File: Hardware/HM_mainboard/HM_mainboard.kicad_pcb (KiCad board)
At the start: 2 copper layers, 80 x 55 mm, 58 parts, among them J1 JST PH2P ST90, J2 USB4105-GF-A, J3 Conn_01x04, J4 54-00174, J5 54-00174, J6 54-00174, J7 54-00174, Q1 PMOS AS3401, U1 MCP73831-2, U2 TC1262-33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

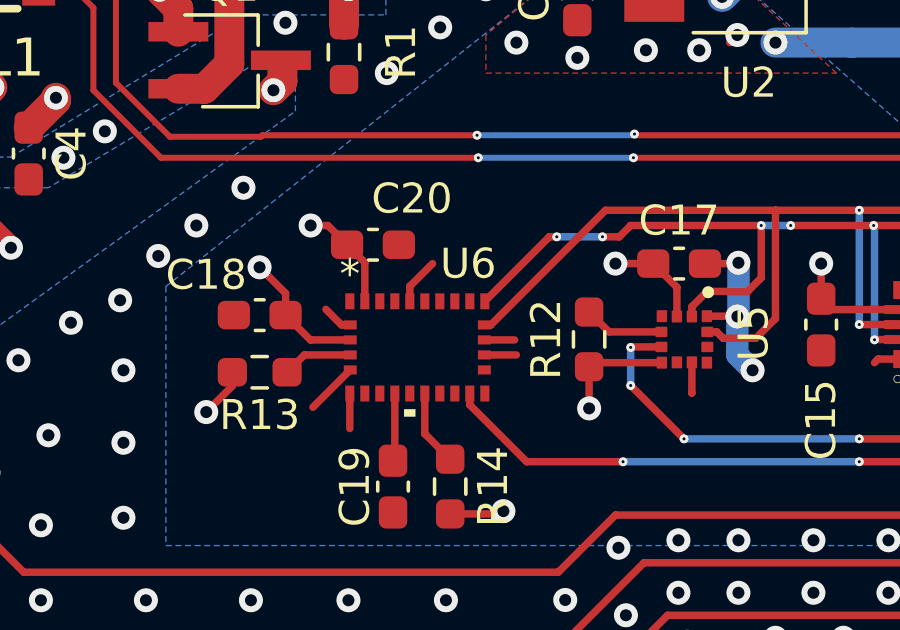
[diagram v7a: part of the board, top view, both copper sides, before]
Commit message: Fixed missing GND connections of BNO055 at Pin 15 and 16
Bugfix due to wrong pin assignments in symbol library
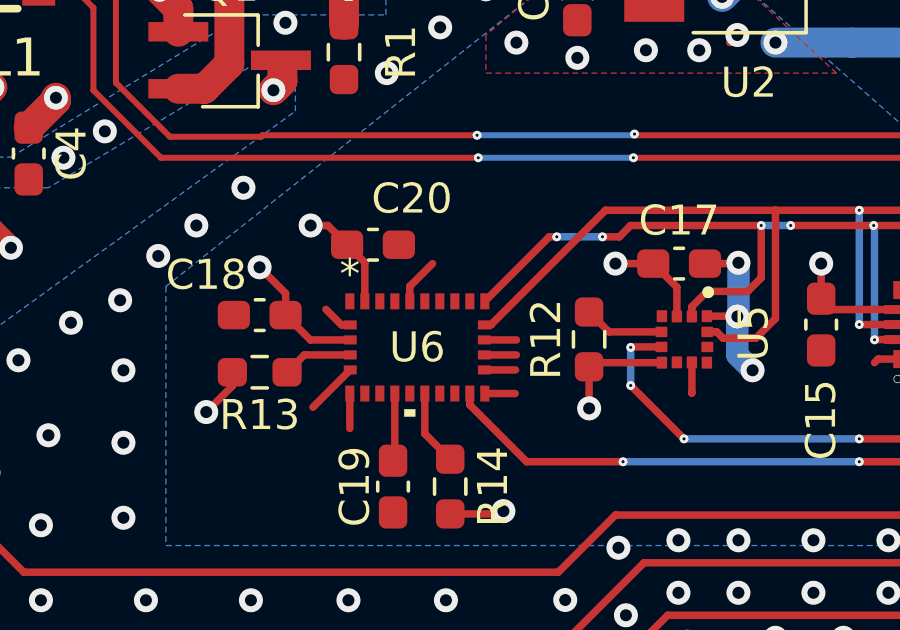
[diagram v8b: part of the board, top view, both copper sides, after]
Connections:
- U6 pad 15: unconnected-(U6-NC-Pad15) -> GND
- U6 pad 16: unconnected-(U6-NC-Pad16) -> GND
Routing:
- net GND: track 30.7 -> 32.8 mm
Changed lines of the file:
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@@
   (net 73 "unconnected-(U6-NC-Pad12)")
   (net 74 "unconnected-(U6-NC-Pad13)")
-  (net 75 "unconnected-(U6-NC-Pad15)")
-  (net 76 "unconnected-(U6-NC-Pad16)")
-  (net 77 "unconnected-(U6-NC-Pad21)")
-  (net 78 "unconnected-(U6-NC-Pad22)")
-  (net 79 "unconnected-(U6-NC-Pad23)")
-  (net 80 "unconnected-(U6-NC-Pad24)")
-  (net 81 "unconnected-(U6-XOUT32-Pad26)")
-  (net 82 "unconnected-(U6-XIN32-Pad27)")
+  (net 75 "unconnected-(U6-NC-Pad21)")
+  (net 76 "unconnected-(U6-NC-Pad22)")
+  (net 77 "unconnected-(U6-NC-Pad23)")
+  (net 78 "unconnected-(U6-NC-Pad24)")
+  (net 79 "unconnected-(U6-XOUT32-Pad26)")
+  (net 80 "unconnected-(U6-XIN32-Pad27)")
   (footprint "Capacitor_SMD:C_0603_1608Metric_Pad1.08x0.95mm_HandSolder" (layer "F.Cu")
     (at 166.116 99.06 90)
@@
     (property "ki_keywords" "BNO055")
     (attr smd)
-    (fp_text reference "U6" (at 1.697499 -2.7883 unlocked) (layer "F.SilkS")
+    (fp_text reference "U6" (at 0 0 unlocked) (layer "F.SilkS")
         (effects (font (size 1 1) (thickness 0.15)))
     )
@@
       (net 51 "/BNO55_INT") (pinfunction "INT") (pintype "output"))
     (pad "15" smd rect (at 2.249999 1.5367) (size 0.3048 0.5334) (layers "F.Cu" "F.Paste" "F.Mask")
-      (net 75 "unconnected-(U6-NC-Pad15)") (pinfunction "NC") (pintype "no_connect"))
+      (net 1 "GND") (pinfunction "Pin15") (pintype "power_out"))
     (pad "16" smd rect (at 2.2352 0.750001 90) (size 0.3048 0.4318) (layers "F.Cu" "F.Paste" "F.Mask")
-      (net 76 "unconnected-(U6-NC-Pad16)") (pinfunction "NC") (pintype "no_connect"))
+      (net 1 "GND") (pinfunction "Pin16") (pintype "power_out"))
     (pad "17" smd rect (at 2.2352 0.25 90) (size 0.3048 0.4318) (layers "F.Cu" "F.Paste" "F.Mask")
       (net 1 "GND") (pinfunction "COM3") (pintype "input"))
@@
       (net 8 "/I2C_SDA") (pinfunction "COM0") (pintype "bidirectional"))
     (pad "21" smd rect (at 1.749999 -1.5367) (size 0.3048 0.5334) (layers "F.Cu" "F.Paste" "F.Mask")
-      (net 77 "unconnected-(U6-NC-Pad21)") (pinfunction "NC") (pintype "no_connect"))
+      (net 75 "unconnected-(U6-NC-Pad21)") (pinfunction "NC") (pintype "no_connect"))
     (pad "22" smd rect (at 1.25 -1.5367) (size 0.3048 0.5334) (layers "F.Cu" "F.Paste" "F.Mask")
-      (net 78 "unconnected-(U6-NC-Pad22)") (pinfunction "NC") (pintype "no_connect"))
+      (net 76 "unconnected-(U6-NC-Pad22)") (pinfunction "NC") (pintype "no_connect"))
     (pad "23" smd rect (at 0.750001 -1.5367) (size 0.3048 0.5334) (layers "F.Cu" "F.Paste" "F.Mask")
-      (net 79 "unconnected-(U6-NC-Pad23)") (pinfunction "NC") (pintype "no_connect"))
+      (net 77 "unconnected-(U6-NC-Pad23)") (pinfunction "NC") (pintype "no_connect"))
     (pad "24" smd rect (at 0.25 -1.5367) (size 0.3048 0.5334) (layers "F.Cu" "F.Paste" "F.Mask")
-      (net 80 "unconnected-(U6-NC-Pad24)") (pinfunction "NC") (pintype "no_connect"))
+      (net 78 "unconnected-(U6-NC-Pad24)") (pinfunction "NC") (pintype "no_connect"))
     (pad "25" smd rect (at -0.25 -1.5367) (size 0.3048 0.5334) (layers "F.Cu" "F.Paste" "F.Mask")
       (net 1 "GND") (pinfunction "GNDIO") (pintype "power_out"))
     (pad "26" smd rect (at -0.750001 -1.5367) (size 0.3048 0.5334) (layers "F.Cu" "F.Paste" "F.Mask")
-      (net 81 "unconnected-(U6-XOUT32-Pad26)") (pinfunction "XOUT32") (pintype "output+no_connect"))
+      (net 79 "unconnected-(U6-XOUT32-Pad26)") (pinfunction "XOUT32") (pintype "output+no_connect"))
     (pad "27" smd rect (at -1.25 -1.5367) (size 0.3048 0.5334) (layers "F.Cu" "F.Paste" "F.Mask")
-      (net 82 "unconnected-(U6-XIN32-Pad27)") (pinfunction "XIN32") (pintype "input+no_connect"))
+      (net 80 "unconnected-(U6-XIN32-Pad27)") (pinfunction "XIN32") (pintype "input+no_connect"))
     (pad "28" smd rect (at -1.749999 -1.5367) (size 0.3048 0.5334) (layers "F.Cu" "F.Paste" "F.Mask")
       (net 3 "3.3V") (pinfunction "VDDIO") (pintype "power_in"))
@@
   (segment (start 156.387 98.78) (end 156.452618 98.78) (width 0.25) (layer "F.Cu") (net 1))
   (segment (start 154.948 100.32) (end 154.948 101.338) (width 0.25) (layer "F.Cu") (net 1))
-  (segment (start 148.0312 99.572) (end 149.0392 99.572) (width 0.25) (layer "F.Cu") (net 1))
   (segment (start 129.921 94.963) (end 129.921 96.421) (width 0.25) (layer "F.Cu") (net 1))
   (segment (start 161.156 100.21) (end 161.036 100.33) (width 0.25) (layer "F.Cu") (net 1))
@@
   (segment (start 164.846 98.806) (end 164.592 99.06) (width 0.25) (layer "F.Cu") (net 1))
   (segment (start 148.0312 100.072) (end 149.098 100.072) (width 0.25) (layer "F.Cu") (net 1))
+  (segment (start 148.045999 101.3587) (end 149.0587 101.3587) (width 0.25) (layer "F.Cu") (net 1))
   (segment (start 156.452618 98.78) (end 156.464 98.791382) (width 0.25) (layer "F.Cu") (net 1))
   (segment (start 188.976 83.82) (end 187.405 85.391) (width 0.25) (layer "F.Cu") (net 1))
@@
   (segment (start 156.472 97.028) (end 156.5 97) (width 0.25) (layer "F.Cu") (net 1))
   (segment (start 126.975 80.515) (end 126.43 80.515) (width 0.5) (layer "F.Cu") (net 1))
+  (segment (start 148.0312 99.572) (end 149.1 99.572) (width 0.25) (layer "F.Cu") (net 1))
   (segment (start 126.43 80.515) (end 125.855 79.94) (width 0.5) (layer "F.Cu") (net 1))
   (segment (start 124.394 99.281) (end 124.394 98.138) (width 1) (layer "F.Cu") (net 1))
   (segment (start 154.948 101.338) (end 154.94 101.346) (width 0.25) (layer "F.Cu") (net 1))
+  (segment (start 148.0312 100.572001) (end 149.072001 100.572001) (width 0.25) (layer "F.Cu") (net 1))
   (via (at 132.5 100.25) (size 0.8) (drill 0.4) (layers "F.Cu" "B.Cu") (free) (net 1))
   (via (at 148 80.75) (size 0.8) (drill 0.4) (layers "F.Cu" "B.Cu") (free) (net 1))
